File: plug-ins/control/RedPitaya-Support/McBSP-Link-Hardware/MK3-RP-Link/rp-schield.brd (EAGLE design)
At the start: 59 x 55.3 mm, 18 parts, among them U1 SN65MLVD202A, U2 SN65MLVD202A, U3 SN65MLVD202A

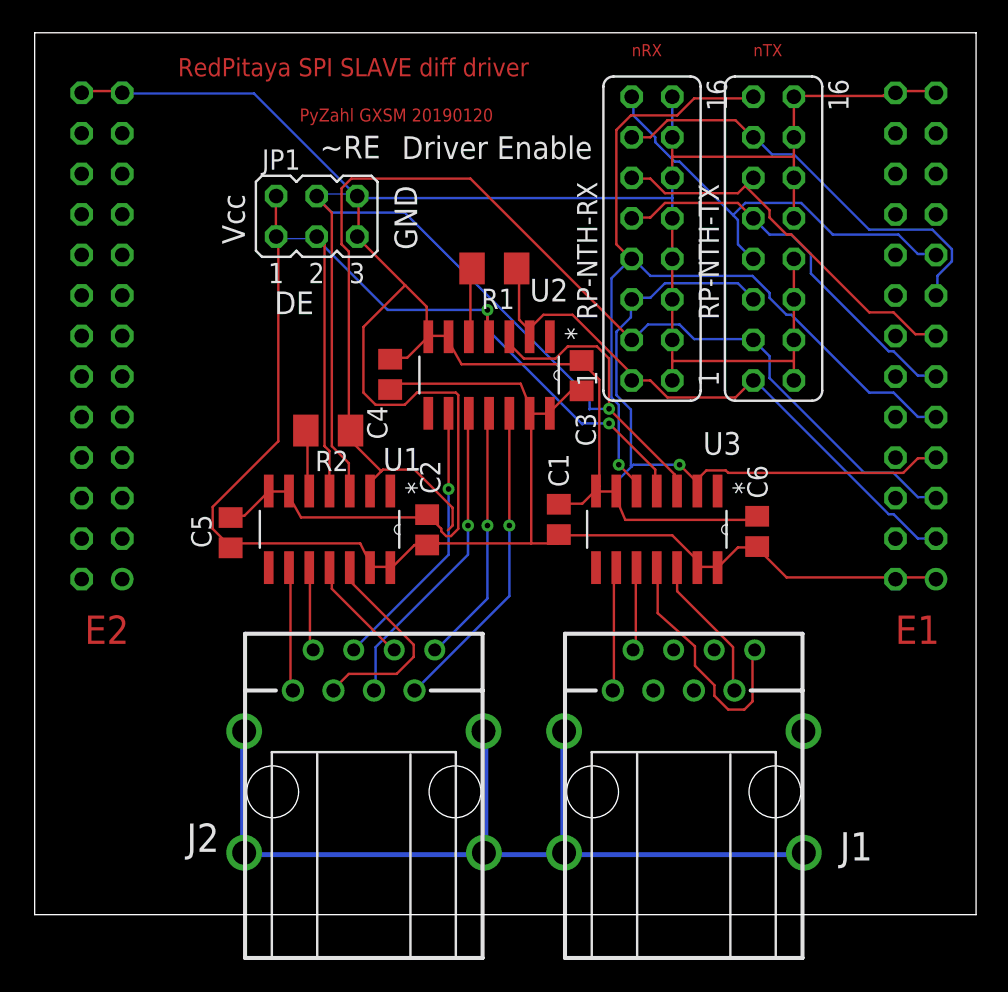
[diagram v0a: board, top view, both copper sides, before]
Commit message: updated gnd routing
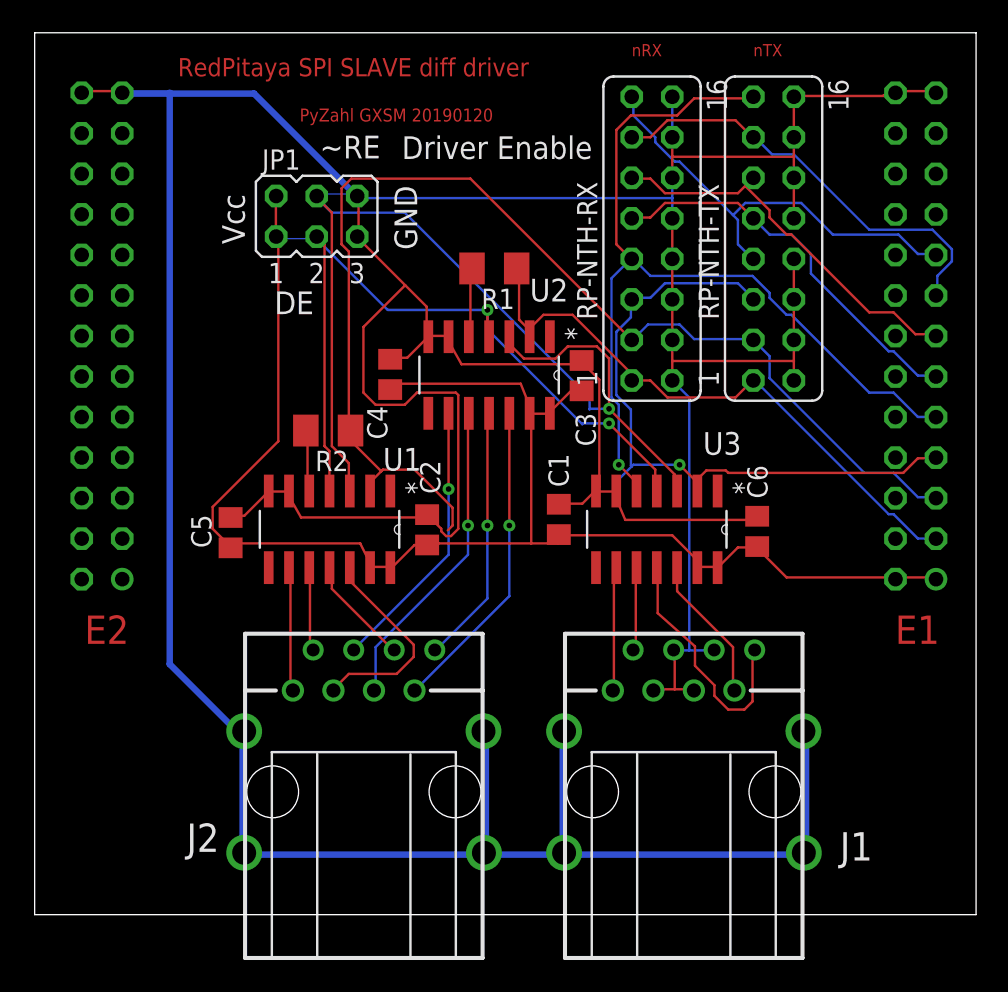
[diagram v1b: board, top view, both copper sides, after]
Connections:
- net GND: now also J1.3, J1.4, J1.5, J1.6
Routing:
- net N$1: track 50.5 -> 103.3 mm
- net GND: track 186.0 -> 211.0 mm
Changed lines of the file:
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@@
 <wire x1="5.0292" y1="56.2356" x2="4.898825" y2="56.128228125" width="0.1524" layer="1"/>
 <wire x1="7.3152" y1="56.2356" x2="7.438825" y2="56.128228125" width="0.1524" layer="1"/>
-<wire x1="15.6972" y1="56.0832" x2="7.4676" y2="56.0832" width="0.1524" layer="16"/>
-<wire x1="22.098" y1="49.6824" x2="15.6972" y2="56.0832" width="0.1524" layer="16"/>
+<wire x1="15.6972" y1="56.0832" x2="7.4676" y2="56.0832" width="0.4064" layer="16"/>
+<wire x1="22.098" y1="49.6824" x2="15.6972" y2="56.0832" width="0.4064" layer="16"/>
 <wire x1="7.4676" y1="56.0832" x2="7.438825" y2="56.128228125" width="0.1524" layer="16"/>
 <wire x1="22.098" y1="49.6824" x2="22.16563125" y2="49.657715625" width="0.1524" layer="16"/>
@@
 <wire x1="22.2504" y1="49.53" x2="41.91" y2="49.53" width="0.1524" layer="16"/>
 <wire x1="22.2504" y1="49.53" x2="22.16563125" y2="49.657715625" width="0.1524" layer="16"/>
+<contactref element="J1" pad="3"/>
+<contactref element="J1" pad="4"/>
+<contactref element="J1" pad="5"/>
+<contactref element="J1" pad="6"/>
+<wire x1="44.5008" y1="21.1836" x2="42.9768" y2="21.1836" width="0.1524" layer="16"/>
+<wire x1="42.9768" y1="21.1836" x2="42.0624" y2="21.1836" width="0.1524" layer="16"/>
+<wire x1="42.0624" y1="21.1836" x2="41.995" y2="21.21" width="0.1524" layer="16"/>
+<wire x1="44.5008" y1="21.1836" x2="44.535" y2="21.21" width="0.1524" layer="16"/>
+<wire x1="43.1292" y1="18.7452" x2="42.0624" y2="18.7452" width="0.1524" layer="1"/>
+<wire x1="42.0624" y1="18.7452" x2="40.8432" y2="18.7452" width="0.1524" layer="1"/>
+<wire x1="40.8432" y1="18.7452" x2="40.725" y2="18.67" width="0.1524" layer="1"/>
+<wire x1="43.1292" y1="18.7452" x2="43.265" y2="18.67" width="0.1524" layer="1"/>
+<wire x1="42.0624" y1="18.7452" x2="42.0624" y2="21.1836" width="0.1524" layer="1"/>
+<wire x1="42.0624" y1="21.1836" x2="41.995" y2="21.21" width="0.1524" layer="1"/>
+<wire x1="42.9768" y1="37.0332" x2="42.9768" y2="21.1836" width="0.1524" layer="16"/>
+<wire x1="41.91" y1="38.1" x2="42.9768" y2="37.0332" width="0.1524" layer="16"/>
 </signal>
 <signal name="FPGA-S-CLK">
@@
 <wire x1="20.4216" y1="31.2928" x2="20.43" y2="31.1706" width="0.1524" layer="1"/>
 <wire x1="19.6596" y1="46.99" x2="19.62563125" y2="47.117715625" width="0.1524" layer="16"/>
-<wire x1="30.3276" y1="41.3512" x2="30.3276" y2="41.3004" width="0.1524" layer="1"/>
 <wire x1="30.3276" y1="41.3004" x2="30.3276" y2="40.894" width="0.1524" layer="1"/>
 <wire x1="30.3276" y1="40.894" x2="30.43" y2="40.8406" width="0.1524" layer="1"/>
@@
 <wire x1="40.8432" y1="31.2928" x2="40.94" y2="31.1706" width="0.1524" layer="1"/>
 <via x="37.9476" y="35.4076" extent="1-16" drill="0.35"/>
-<wire x1="30.3276" y1="42.5196" x2="30.3276" y2="41.3512" width="0.1524" layer="1"/>
+<wire x1="30.3276" y1="42.5196" x2="30.3276" y2="41.3004" width="0.1524" layer="1"/>
 <wire x1="30.3276" y1="41.3004" x2="30.3276" y2="42.5196" width="0.1524" layer="16"/>
 <wire x1="36.2712" y1="35.3568" x2="30.3276" y2="41.3004" width="0.1524" layer="16"/>
@@
 </signal>
 <signal name="N$1">
-<wire x1="14.986" y1="16.002" x2="14.986" y2="8.636" width="0.3048" layer="16"/>
+<wire x1="14.986" y1="16.002" x2="14.986" y2="15.748" width="0.3048" layer="16"/>
+<wire x1="14.986" y1="15.748" x2="14.986" y2="8.636" width="0.4064" layer="16"/>
 <wire x1="14.986" y1="8.636" x2="15.24" y2="8.382" width="0.3048" layer="16"/>
-<wire x1="15.24" y1="8.382" x2="35.052" y2="8.382" width="0.3048" layer="16"/>
-<wire x1="35.052" y1="8.382" x2="50.038" y2="8.382" width="0.3048" layer="16"/>
+<wire x1="15.24" y1="8.382" x2="35.052" y2="8.382" width="0.4064" layer="16"/>
+<wire x1="35.052" y1="8.382" x2="50.038" y2="8.382" width="0.4064" layer="16"/>
 <wire x1="50.038" y1="8.382" x2="50.292" y2="8.636" width="0.3048" layer="16"/>
-<wire x1="35.052" y1="8.382" x2="35.052" y2="16.002" width="0.3048" layer="16"/>
+<wire x1="35.052" y1="8.382" x2="35.052" y2="16.002" width="0.4064" layer="16"/>
+<wire x1="14.986" y1="15.748" x2="10.414" y2="20.32" width="0.4064" layer="16"/>
+<wire x1="10.414" y1="20.32" x2="10.414" y2="56.134" width="0.4064" layer="16"/>
+<wire x1="10.414" y1="56.134" x2="7.366" y2="56.134" width="0.254" layer="16"/>
+<wire x1="50.292" y1="8.636" x2="50.292" y2="15.494" width="0.4064" layer="16"/>
+<wire x1="50.292" y1="15.494" x2="50.038" y2="15.748" width="0.4064" layer="16"/>
+<wire x1="50.038" y1="15.748" x2="50.038" y2="15.494" width="0.4064" layer="16"/>
 </signal>
 <signal name="N$3">
 <wire x1="29.972" y1="8.128" x2="30.226" y2="8.382" width="0.3048" layer="16"/>
-<wire x1="30.226" y1="8.382" x2="30.226" y2="16.002" width="0.3048" layer="16"/>
+<wire x1="30.226" y1="8.382" x2="30.226" y2="16.002" width="0.4064" layer="16"/>
 </signal>
 <signal name="FSP">

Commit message: updated MK3 Link Design Files, added detailed BOM (xlsx)
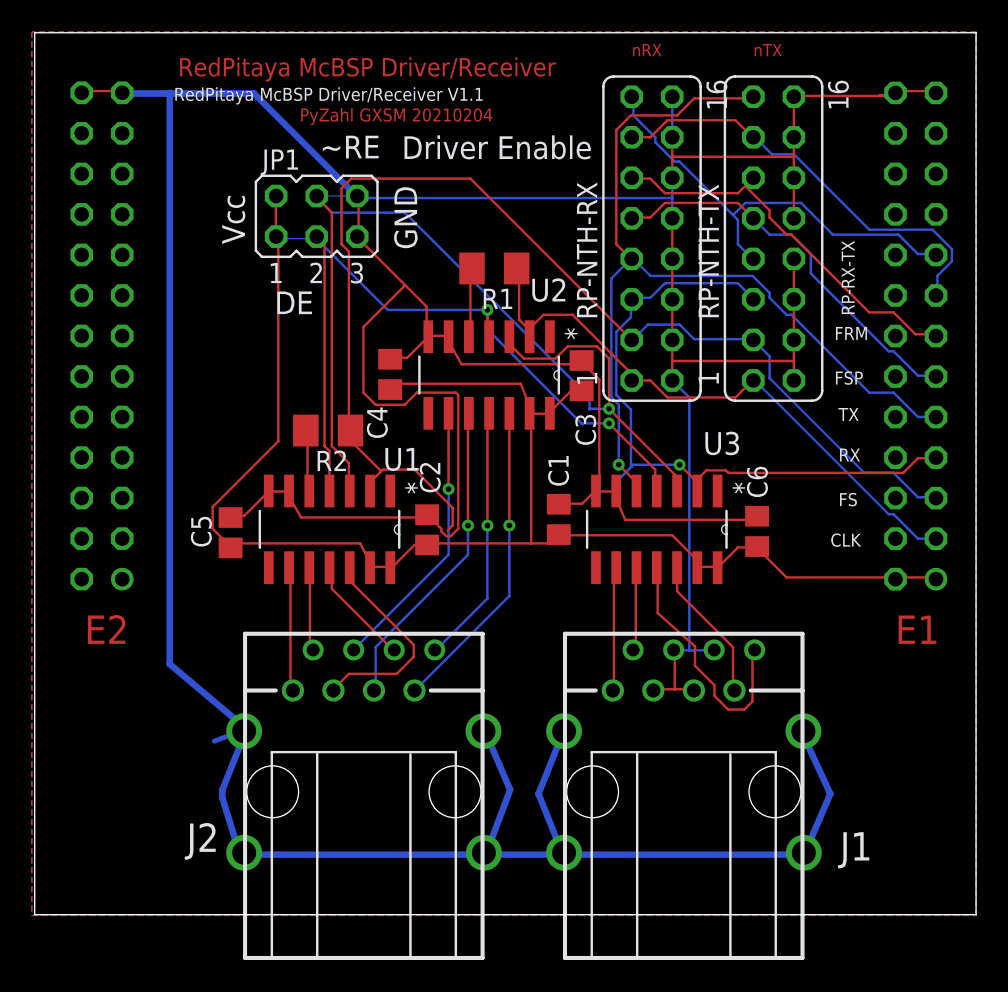
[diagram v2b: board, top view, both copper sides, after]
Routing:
- net GND: track 211.0 -> 329.5 mm, vias 3 -> 0
- net N$1: track 103.3 -> 0.00 mm
- net N$3: track 7.98 -> 0.00 mm
- net N$4: track 1.78 -> 0.00 mm
- net VCC: track 0.00 -> 1.52 mm
- net N$5: track 1.52 -> 0.00 mm
- net VCC+3.3V: track 97.1 -> 97.8 mm, vias 3 -> 0
- added copper zone on layer 1, net GND
- added copper zone on layer 16, net GND
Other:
- board text added: "CLK"
- board text added: "FRM"
- board text added: "FS"
- board text added: "FSP"
- board text added: "PyZahl GXSM 20210204"
- board text added: "RP-RX-TX"
- board text added: "RX"
- board text added: "RedPitaya McBSP Driver/Receiver"
- board text added: "RedPitaya McBSP Driver/Receiver V1.1"
- board text added: "TX"
- board text removed: "PyZahl GXSM 20190120"
- board text removed: "RedPitaya SPI SLAVE diff driver"

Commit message: added next version and support material
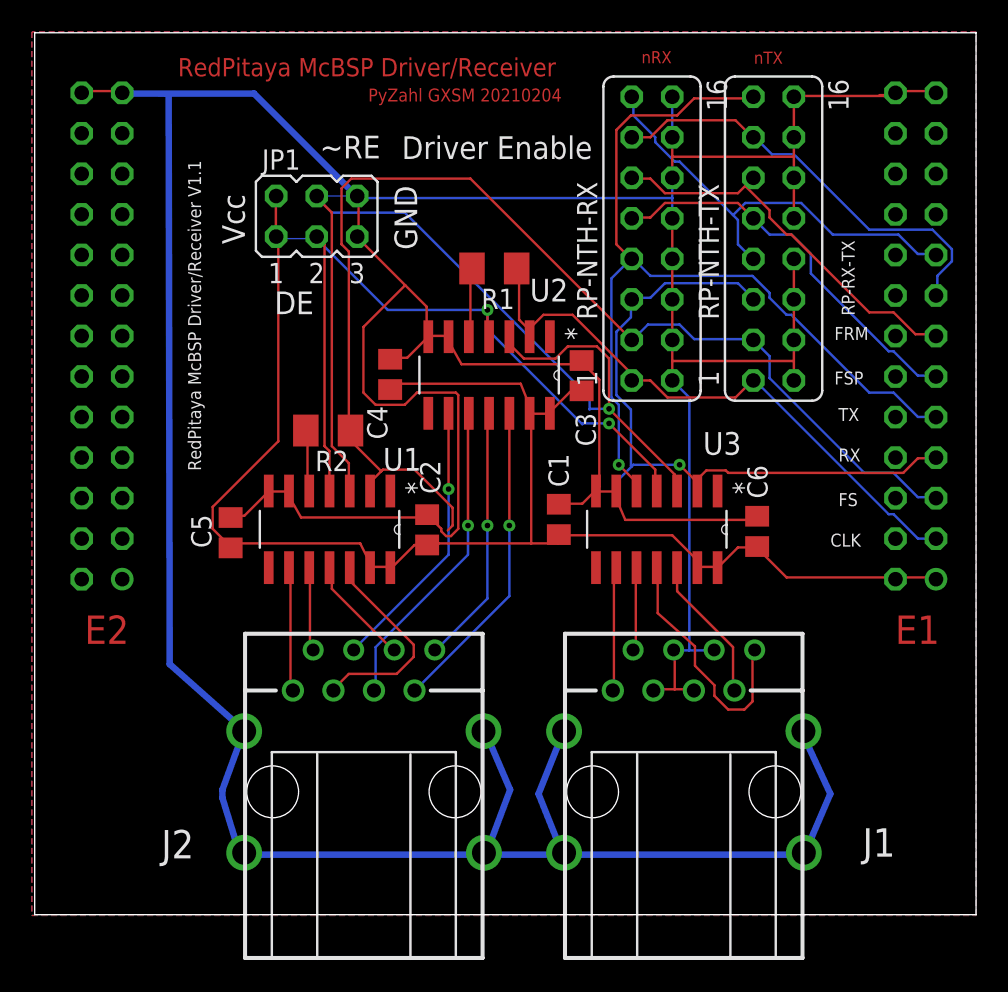
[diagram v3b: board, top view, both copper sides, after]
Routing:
- net GND: track 329.5 -> 327.1 mm
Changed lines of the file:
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@@
 <text x="15.12481875" y="46.64525" size="1.4224" layer="25" rot="R90">Vcc</text>
 <text x="10.92645" y="57.160878125" size="1.143" layer="1">RedPitaya McBSP Driver/Receiver</text>
-<text x="18.55498125" y="54.329425" size="0.8128" layer="1">PyZahl GXSM 20210204</text>
+<text x="22.852903125" y="55.5819375" size="0.8128" layer="1">PyZahl GXSM 20210204</text>
 <text x="24.956915625" y="51.979740625" size="1.4224" layer="21">Driver Enable</text>
 <text x="55.88" y="21.59" size="1.778" layer="1">E1</text>
 <text x="5.08" y="21.59" size="1.778" layer="1">E2</text>
-<text x="46.99" y="58.42" size="0.762" layer="1">nTX</text>
-<text x="39.37" y="58.42" size="0.762" layer="1">nRX</text>
-<text x="10.668" y="55.626" size="0.8128" layer="25">RedPitaya McBSP Driver/Receiver V1.1</text>
+<text x="47.023840625" y="57.946075" size="0.762" layer="1">nTX</text>
+<text x="39.97915625" y="57.979928125" size="0.762" layer="1">nRX</text>
+<text x="12.37841875" y="32.4377625" size="0.8128" layer="25" rot="R90">RedPitaya McBSP Driver/Receiver V1.1</text>
 <text x="52.324" y="35.56" size="0.8128" layer="25">TX</text>
 <text x="52.324" y="33.02" size="0.8128" layer="25">RX</text>
@@
 </element>
 <element name="J1" library="con-amp-rj45-shield" package="557785-1" value="" x="42.63" y="12.32" smashed="yes">
-<attribute name="NAME" x="54.461021875" y="9.79126875" size="1.778" layer="25" rot="R180"/>
+<attribute name="NAME" x="55.882265625" y="10.0350625" size="1.778" layer="25" rot="R180"/>
 <attribute name="VALUE" x="52.282" y="7.494" size="1.778" layer="27" rot="R90"/>
 </element>
 <element name="J2" library="con-amp-rj45-shield" package="557785-1" value="" x="22.58" y="12.32" smashed="yes">
-<attribute name="NAME" x="13.516609375" y="10.332359375" size="1.778" layer="25" rot="R180"/>
+<attribute name="NAME" x="11.932940625" y="9.9260375" size="1.778" layer="25" rot="R180"/>
 <attribute name="VALUE" x="32.232" y="7.494" size="1.778" layer="27" rot="R90"/>
 </element>
@@
 <attribute name="PACKAGE" value="SOIC-14" x="16.62" y="26.37" size="1.778" layer="27" rot="R270" display="off"/>
 <attribute name="SUPPLIER" value="TEXAS INSTRUMENTS" x="16.62" y="26.37" size="1.778" layer="27" rot="R270" display="off"/>
-<attribute name="VALUE" x="13.389871875" y="23.12738125" size="1.4224" layer="27" ratio="10" rot="SR0"/>
+<attribute name="VALUE" x="16.63869375" y="23.8044125" size="0.8128" layer="27" ratio="10" rot="SR0"/>
 </element>
 <element name="U2" library="Texas Instruments_By_element14_Batch_1" package="SOIC127P600X175-14N" value="SN65MLVD202A" x="26.62" y="36.04" smashed="yes" rot="R270">
@@
 <attribute name="PACKAGE" value="SOIC-14" x="26.62" y="36.04" size="1.778" layer="27" rot="R270" display="off"/>
 <attribute name="SUPPLIER" value="TEXAS INSTRUMENTS" x="26.62" y="36.04" size="1.778" layer="27" rot="R270" display="off"/>
-<attribute name="VALUE" x="10.088896875" y="40.147759375" size="1.4224" layer="27" ratio="10" rot="SR0"/>
+<attribute name="VALUE" x="26.671428125" y="33.919053125" size="0.8128" layer="27" ratio="10" rot="SR0"/>
 </element>
 <element name="U3" library="Texas Instruments_By_element14_Batch_1" package="SOIC127P600X175-14N" value="SN65MLVD202A" x="37.13" y="26.37" smashed="yes" rot="R270">
@@
 <attribute name="PACKAGE" value="SOIC-14" x="37.13" y="26.37" size="1.778" layer="27" rot="R270" display="off"/>
 <attribute name="SUPPLIER" value="TEXAS INSTRUMENTS" x="37.13" y="26.37" size="1.778" layer="27" rot="R270" display="off"/>
-<attribute name="VALUE" x="34.15569375" y="23.168153125" size="1.4224" layer="27" ratio="10" rot="SR0"/>
+<attribute name="VALUE" x="37.099940625" y="23.70978125" size="0.8128" layer="27" ratio="10" rot="SR0"/>
 </element>
 <element name="JP1" library="jumper" library_urn="urn:adsk.eagle:library:252" package="JP3Q" package3d_urn="urn:adsk.eagle:package:15460/1" value="" x="19.62563125" y="48.387715625"/>
@@
 <vertex x="1.778" y="4.572"/>
 </polygon>
-<wire x1="13.208" y1="15.494" x2="15.24" y2="16.256" width="0.3048" layer="16"/>
-<wire x1="15.24" y1="16.256" x2="13.716" y2="12.446" width="0.4064" layer="16"/>
+<wire x1="15.01705625" y1="16.316484375" x2="15.076871875" y2="16.174434375" width="0.3048" layer="16"/>
+<wire x1="15.076871875" y1="16.174434375" x2="13.716" y2="12.446" width="0.4064" layer="16"/>
 <wire x1="13.716" y1="12.446" x2="13.716" y2="11.938" width="0.4064" layer="16"/>
 <wire x1="13.716" y1="11.938" x2="14.732" y2="8.636" width="0.4064" layer="16"/>
@@
 <wire x1="35.052" y1="8.382" x2="33.528" y2="12.192" width="0.4064" layer="16"/>
 <wire x1="33.528" y1="12.192" x2="35.052" y2="16.002" width="0.4064" layer="16"/>
-<wire x1="15.24" y1="16.256" x2="10.414" y2="20.32" width="0.4064" layer="16"/>
-<wire x1="10.414" y1="20.32" x2="10.414" y2="56.134" width="0.4064" layer="16"/>
-<wire x1="10.414" y1="56.134" x2="7.366" y2="56.134" width="0.254" layer="16"/>
+<wire x1="15.076871875" y1="16.174434375" x2="10.414" y2="20.32" width="0.4064" layer="16"/>
+<wire x1="10.414" y1="20.32" x2="10.34875" y2="55.987159375" width="0.4064" layer="16"/>
+<wire x1="10.34875" y1="55.987159375" x2="7.366" y2="56.134" width="0.254" layer="16"/>
 <wire x1="50.292" y1="8.636" x2="51.816" y2="12.192" width="0.4064" layer="16"/>
 <wire x1="51.816" y1="12.192" x2="50.292" y2="15.494" width="0.4064" layer="16"/>
